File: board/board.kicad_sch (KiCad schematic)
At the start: 3 parts

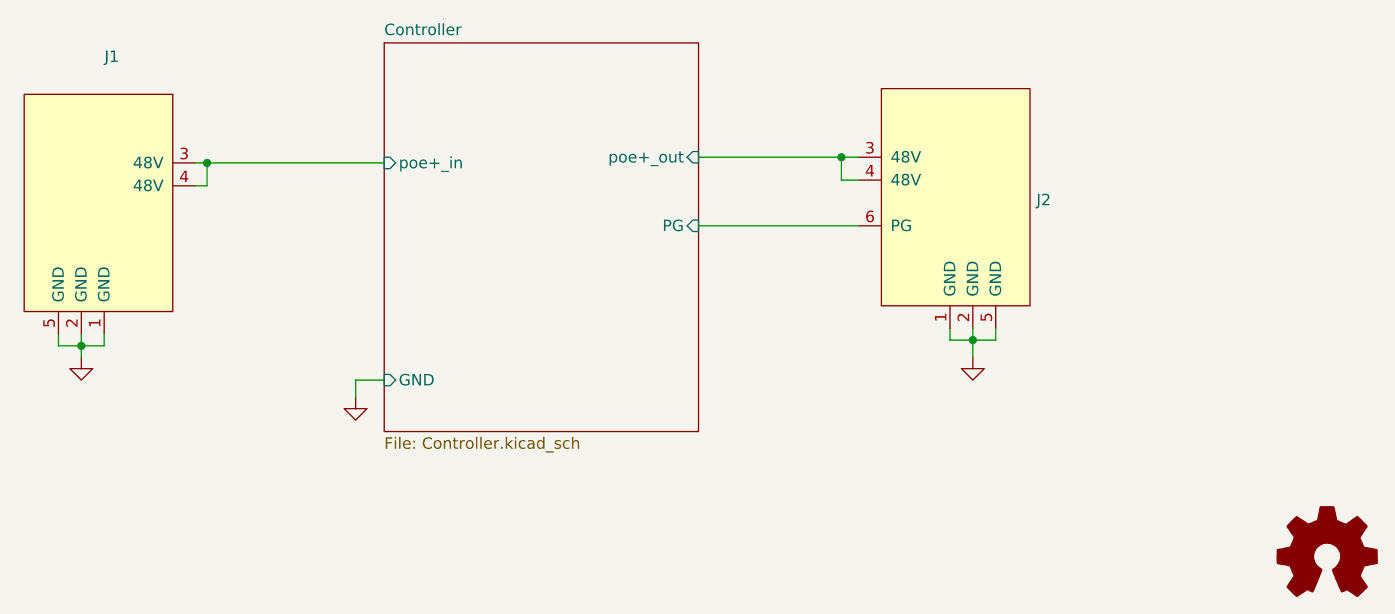
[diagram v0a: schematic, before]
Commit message: changed fp Q1 to back
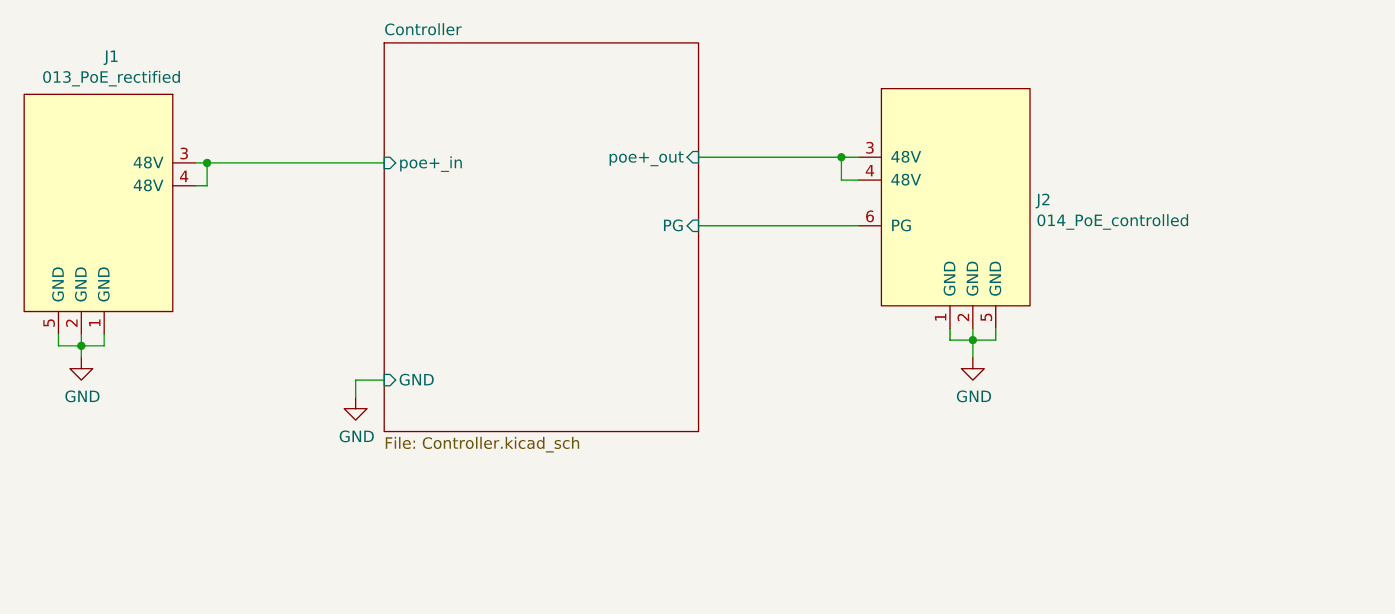
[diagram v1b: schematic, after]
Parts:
- removed LOGO1: (no value), symbol Graphic:Logo_Open_Hardware_Small
- J1: value (none) -> 013_PoE_rectified; footprint (none) -> on_edge:on_edge_2x05_device
- J2: value (none) -> 014_PoE_controlled; footprint (none) -> on_edge:on_edge_2x05_host
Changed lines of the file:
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@@
     (in_bom yes) (on_board yes)
     (property "Reference" "J1" (id 0) (at 88.4682 65.024 0))
-    (property "Value" "" (id 1) (at 88.4682 67.3354 0))
-    (property "Footprint" "" (id 2) (at 78.74 65.405 0)
+    (property "Value" "013_PoE_rectified" (id 1) (at 88.4682 67.3354 0))
+    (property "Footprint" "on_edge:on_edge_2x05_device" (id 2) (at 78.74 65.405 0)
       (effects (font (size 1.27 1.27)) hide)
     )
@@
       (effects (font (size 1.27 1.27)) (justify left))
     )
-    (property "Value" "" (id 1) (at 191.2112 83.2612 0)
+    (property "Value" "014_PoE_controlled" (id 1) (at 191.2112 83.2612 0)
       (effects (font (size 1.27 1.27)) (justify left))
     )
-    (property "Footprint" "" (id 2) (at 190.5 64.77 0)
+    (property "Footprint" "on_edge:on_edge_2x05_host" (id 2) (at 190.5 64.77 0)
       (effects (font (size 1.27 1.27)) hide)
     )
@@
       (effects (font (size 1.27 1.27)) hide)
     )
-    (property "Value" "" (id 1) (at 115.697 107.2642 0))
+    (property "Value" "GND" (id 1) (at 115.697 107.2642 0))
     (property "Footprint" "" (id 2) (at 115.57 102.87 0)
       (effects (font (size 1.27 1.27)) hide)
@@
       (effects (font (size 1.27 1.27)) hide)
     )
-    (property "Value" "" (id 1) (at 85.217 102.8192 0))
+    (property "Value" "GND" (id 1) (at 85.217 102.8192 0))
     (property "Footprint" "" (id 2) (at 85.09 98.425 0)
       (effects (font (size 1.27 1.27)) hide)
@@
       (effects (font (size 1.27 1.27)) hide)
     )
-    (property "Value" "" (id 1) (at 184.277 102.8192 0))
+    (property "Value" "GND" (id 1) (at 184.277 102.8192 0))
     (property "Footprint" "" (id 2) (at 184.15 98.425 0)
       (effects (font (size 1.27 1.27)) hide)
@@
     )
     (pin "1")
-  )
-  (symbol (lib_id "Graphic:Logo_Open_Hardware_Small") (at 223.52 120.65 0) (unit 1)
-    (in_bom yes) (on_board yes)
-    (property "Reference" "LOGO1" (id 0) (at 223.52 113.665 0)
-      (effects (font (size 1.27 1.27)) hide)
-    )
-    (property "Value" "" (id 1) (at 223.52 126.365 0)
-      (effects (font (size 1.27 1.27)) hide)
-    )
-    (property "Footprint" "" (id 2) (at 223.52 120.65 0)
-      (effects (font (size 1.27 1.27)) hide)
-    )
-    (property "Datasheet" "~" (id 3) (at 223.52 120.65 0)
-      (effects (font (size 1.27 1.27)) hide)
-    )
   )
   (sheet (at 118.745 63.5) (size 34.925 43.18) (fields_autoplaced)
@@
       (reference "J2") (unit 1) (value "014_PoE_controlled") (footprint "on_edge:on_edge_2x05_host")
     )
-    (path "/00000000-0000-0000-0000-000061a93476"
-      (reference "LOGO1") (unit 1) (value "Logo_Open_Hardware_Small") (footprint "Symbol:OSHW-Logo2_9.8x8mm_SilkScreen")
-    )
     (path "/00000000-0000-0000-0000-00006083c3a8/00000000-0000-0000-0000-000060842bb2"
-      (reference "Q1") (unit 1) (value "PSMN5R2-60YL") (footprint "Package_TO_SOT_SMD:LFPAK33")
+      (reference "Q1") (unit 1) (value "PSMN5R2-60YL") (footprint "Package_TO_SOT_SMD:LFPAK56")
     )
     (path "/00000000-0000-0000-0000-00006083c3a8/00000000-0000-0000-0000-0000608386ff"

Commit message: updated connectors
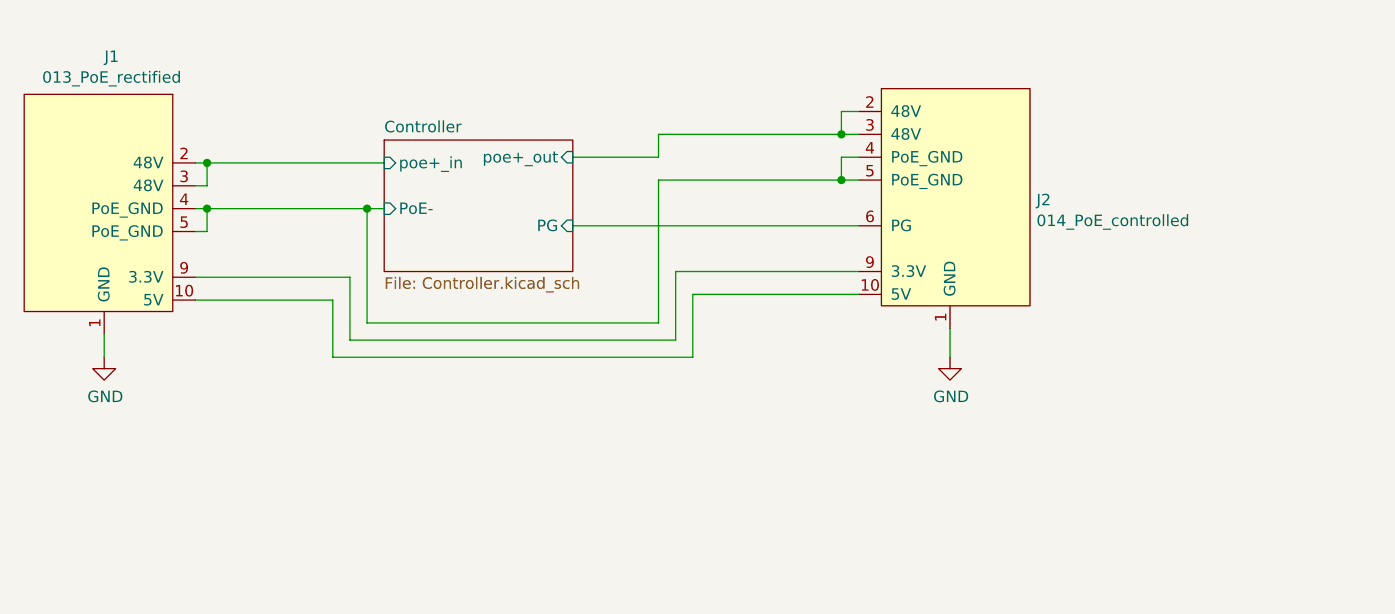
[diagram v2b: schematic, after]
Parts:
- J1: symbol board-rescue:013_PoE_rectified-put_on_edge -> put_on_edge:013_PoE_rectified
- J2: symbol board-rescue:014_PoE_controlled-put_on_edge -> put_on_edge:014_PoE_controlled
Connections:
- net Controller/poe+_in: now also J1.2 (48V); no longer J1.4 (48V)
- net Controller/poe+_out: now also J2.2 (48V); no longer J2.4 (48V)
- net GND: no longer J1.2 (GND), J1.5 (GND), J2.2 (GND), J2.5 (GND)
- new net: J1.10 (5V), J2.10 (5V)
- new net: J1.9 (3.3V), J2.9 (3.3V)
- new net Controller/PoE-: J1.4 (PoE_GND), J1.5 (PoE_GND), J2.4 (PoE_GND), J2.5 (PoE_GND)
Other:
- sheet Controller ports: added PoE-; removed GND

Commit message: added power doo cinnection upstream
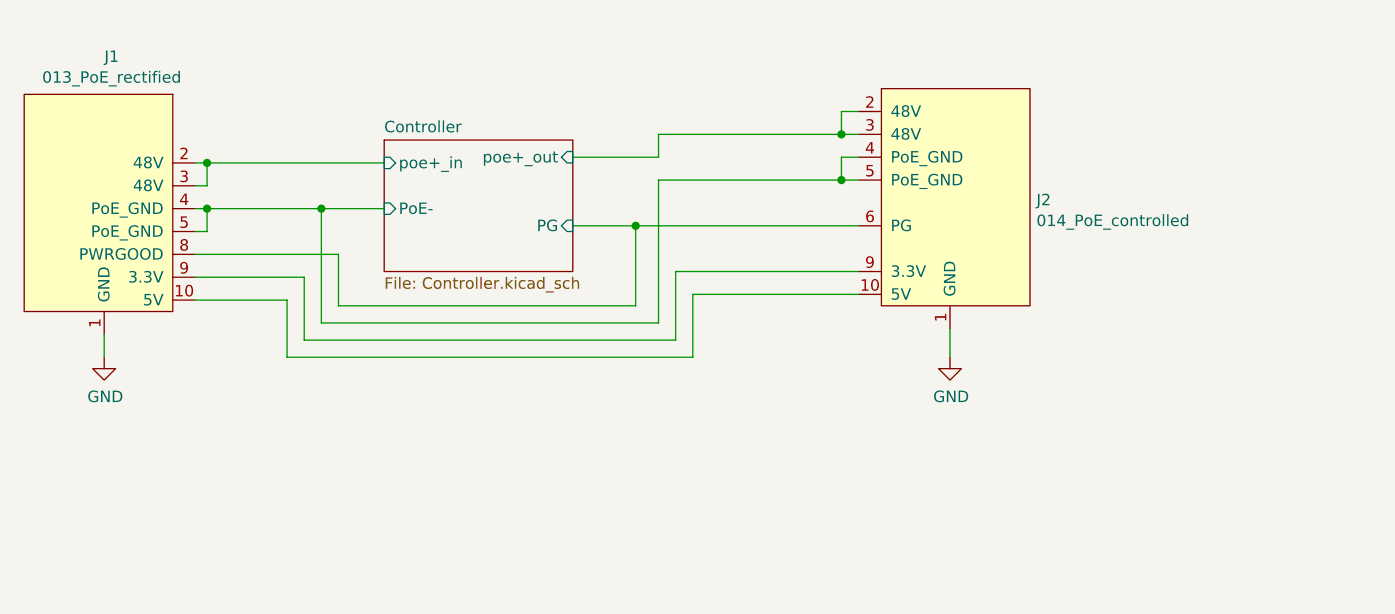
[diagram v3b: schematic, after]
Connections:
- net Controller/PG: now also J1.8 (PWRGOOD)
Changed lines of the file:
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@@
   (junction (at 99.06 76.835) (diameter 0) (color 0 0 0 0)
-  )
-  (junction (at 116.84 81.915) (diameter 0) (color 0 0 0 0)
   )
   (junction (at 99.06 81.915) (diameter 0) (color 0 0 0 0)
   )
   (junction (at 169.545 73.66) (diameter 0) (color 0 0 0 0)
+  )
+  (junction (at 146.685 83.82) (diameter 0) (color 0 0 0 0)
+  )
+  (junction (at 111.76 81.915) (diameter 0) (color 0 0 0 0)
   )
   (junction (at 169.545 78.74) (diameter 0) (color 0 0 0 0)
@@
     (stroke (width 0) (type default) (color 0 0 0 0))
   )
-  (wire (pts (xy 153.035 98.425) (xy 113.03 98.425))
+  (wire (pts (xy 153.035 98.425) (xy 107.95 98.425))
+    (stroke (width 0) (type default) (color 0 0 0 0))
+  )
+  (wire (pts (xy 146.685 83.82) (xy 171.45 83.82))
     (stroke (width 0) (type default) (color 0 0 0 0))
   )
   (wire (pts (xy 139.7 76.2) (xy 149.225 76.2))
+    (stroke (width 0) (type default) (color 0 0 0 0))
+  )
+  (wire (pts (xy 113.665 86.995) (xy 113.665 92.71))
     (stroke (width 0) (type default) (color 0 0 0 0))
   )
@@
   )
   (wire (pts (xy 169.545 76.2) (xy 171.45 76.2))
+    (stroke (width 0) (type default) (color 0 0 0 0))
+  )
+  (wire (pts (xy 113.665 92.71) (xy 146.685 92.71))
     (stroke (width 0) (type default) (color 0 0 0 0))
   )
@@
     (stroke (width 0) (type default) (color 0 0 0 0))
   )
-  (wire (pts (xy 97.79 89.535) (xy 114.935 89.535))
+  (wire (pts (xy 97.79 86.995) (xy 113.665 86.995))
+    (stroke (width 0) (type default) (color 0 0 0 0))
+  )
+  (wire (pts (xy 97.79 89.535) (xy 109.855 89.535))
     (stroke (width 0) (type default) (color 0 0 0 0))
   )
@@
     (stroke (width 0) (type default) (color 0 0 0 0))
   )
-  (wire (pts (xy 139.7 83.82) (xy 171.45 83.82))
+  (wire (pts (xy 139.7 83.82) (xy 146.685 83.82))
     (stroke (width 0) (type default) (color 0 0 0 0))
   )
   (wire (pts (xy 151.13 88.9) (xy 171.45 88.9))
+    (stroke (width 0) (type default) (color 0 0 0 0))
+  )
+  (wire (pts (xy 111.76 81.915) (xy 118.745 81.915))
     (stroke (width 0) (type default) (color 0 0 0 0))
   )
@@
     (stroke (width 0) (type default) (color 0 0 0 0))
   )
-  (wire (pts (xy 113.03 92.075) (xy 97.79 92.075))
+  (wire (pts (xy 107.95 92.075) (xy 97.79 92.075))
     (stroke (width 0) (type default) (color 0 0 0 0))
   )
@@
     (stroke (width 0) (type default) (color 0 0 0 0))
   )
-  (wire (pts (xy 113.03 98.425) (xy 113.03 92.075))
+  (wire (pts (xy 107.95 98.425) (xy 107.95 92.075))
     (stroke (width 0) (type default) (color 0 0 0 0))
   )
@@
     (stroke (width 0) (type default) (color 0 0 0 0))
   )
-  (wire (pts (xy 99.06 81.915) (xy 116.84 81.915))
+  (wire (pts (xy 99.06 81.915) (xy 111.76 81.915))
     (stroke (width 0) (type default) (color 0 0 0 0))
   )
@@
     (stroke (width 0) (type default) (color 0 0 0 0))
   )
-  (wire (pts (xy 114.935 96.52) (xy 151.13 96.52))
+  (wire (pts (xy 109.855 96.52) (xy 151.13 96.52))
     (stroke (width 0) (type default) (color 0 0 0 0))
   )
-  (wire (pts (xy 116.84 94.615) (xy 149.225 94.615))
-    (stroke (width 0) (type default) (color 0 0 0 0))
-  )
-  (wire (pts (xy 116.84 81.915) (xy 118.745 81.915))
+  (wire (pts (xy 111.76 94.615) (xy 149.225 94.615))
     (stroke (width 0) (type default) (color 0 0 0 0))
   )
@@
     (stroke (width 0) (type default) (color 0 0 0 0))
   )
+  (wire (pts (xy 146.685 92.71) (xy 146.685 83.82))
+    (stroke (width 0) (type default) (color 0 0 0 0))
+  )
   (wire (pts (xy 169.545 76.2) (xy 169.545 78.74))
     (stroke (width 0) (type default) (color 0 0 0 0))
   )
-  (wire (pts (xy 114.935 89.535) (xy 114.935 96.52))
+  (wire (pts (xy 109.855 89.535) (xy 109.855 96.52))
     (stroke (width 0) (type default) (color 0 0 0 0))
   )
-  (wire (pts (xy 116.84 81.915) (xy 116.84 94.615))
+  (wire (pts (xy 111.76 81.915) (xy 111.76 94.615))
     (stroke (width 0) (type default) (color 0 0 0 0))
   )
@@
     (pin "4")
     (pin "5")
+    (pin "8")
     (pin "9")
   )
